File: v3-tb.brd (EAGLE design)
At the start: 40.6 x 48.3 mm, 47 parts, among them J1 MPU_SPI, J10 HRDAC, J11 AMPS, J12 CDC_PC, J13 GND, J2 MCU_SPI, J3 MPU_I2C, J4 MPU_ETC, J5 MCU_ETC, J8 RGB_D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

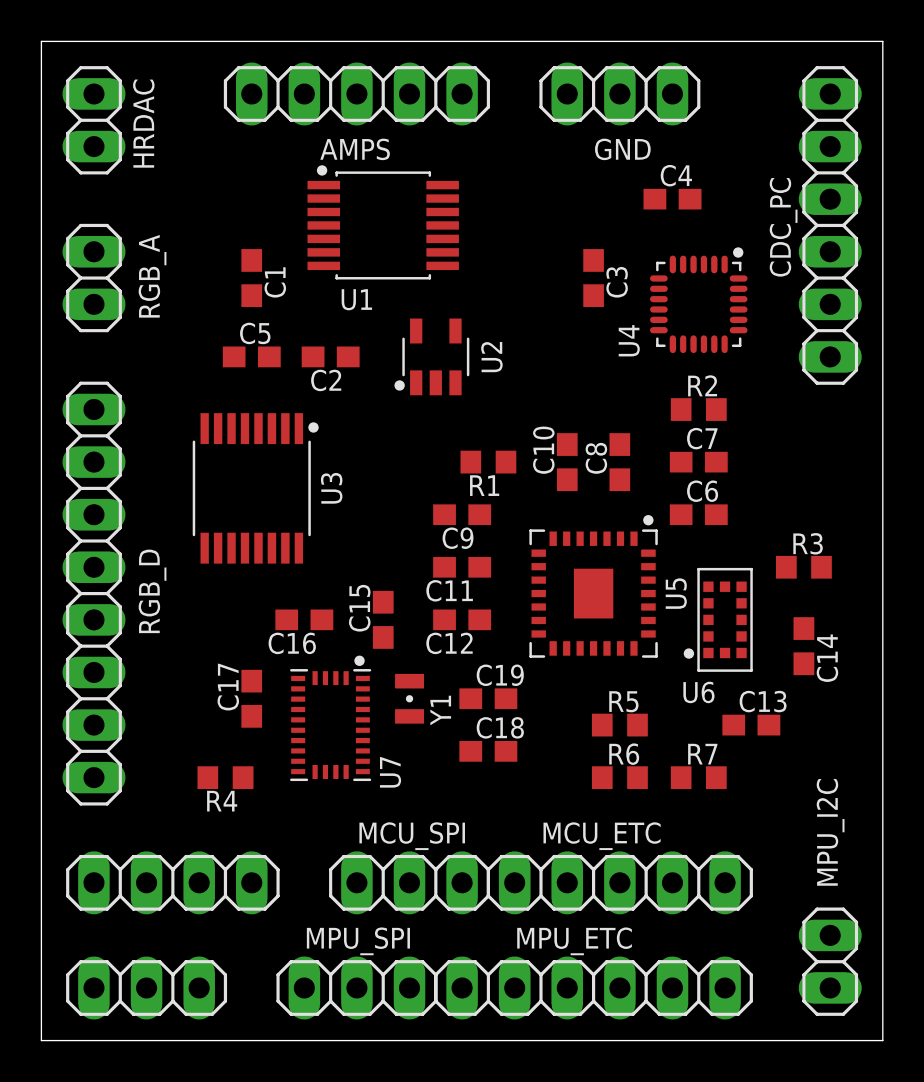
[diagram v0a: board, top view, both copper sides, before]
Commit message: Route as 4layer
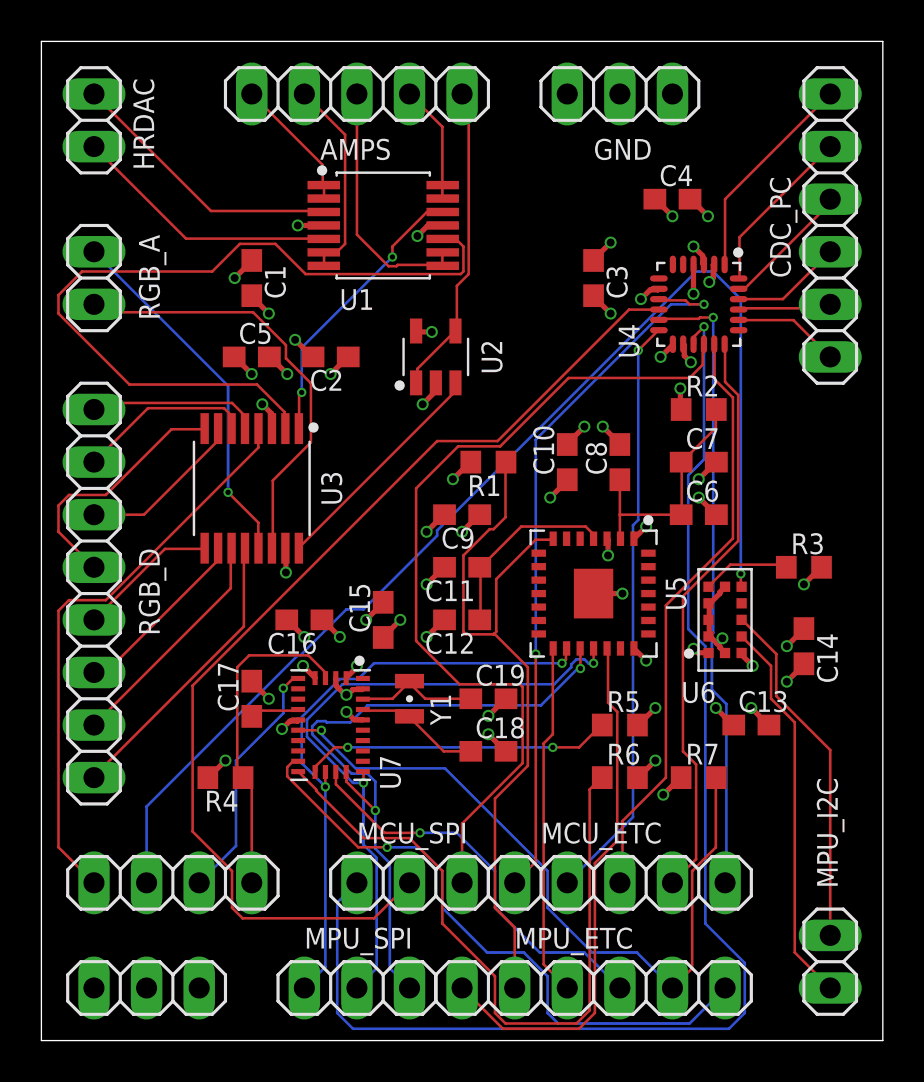
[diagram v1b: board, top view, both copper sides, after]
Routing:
- net GND: track 0.00 -> 176.6 mm, vias 0 -> 32
- net +3V3: track 0.00 -> 163.8 mm, vias 0 -> 26
- net MCU_MOSI: track 0.00 -> 62.7 mm, vias 0 -> 1
- net MPU_TOF_GPIO: track 0.00 -> 57.7 mm, vias 0 -> 1
- net +1V8: track 0.00 -> 52.0 mm, vias 0 -> 3
- net MCU_MISO: track 0.00 -> 51.1 mm
- net MCU_SCK: track 0.00 -> 41.4 mm
- net N$6: track 0.00 -> 38.2 mm
- net MPU_OMT_!RST: track 0.00 -> 35.8 mm
- net MPU_IMU_!RST: track 0.00 -> 35.4 mm, vias 0 -> 1
- net MCU_CDC_!CS: track 0.00 -> 35.0 mm, vias 0 -> 2
- net N$2: track 0.00 -> 33.5 mm
- net MPU_SCK: track 0.00 -> 32.6 mm, vias 0 -> 2
- net MPU_MISO: track 0.00 -> 31.5 mm, vias 0 -> 2
- net MCU_CDC_PG5: track 0.00 -> 30.3 mm, vias 0 -> 1
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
